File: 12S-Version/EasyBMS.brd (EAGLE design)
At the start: 49 x 100 mm, 146 parts, among them IC2 LTC6811IG-1#PBF, Q10 BSS84LT1G, Q11 BSS84LT1G, Q12 BSS84LT1G, Q13 BSS84LT1G, Q2 BSS84LT1G, Q3 BSS84LT1G, Q4 BSS84LT1G, Q5 BSS84LT1G, Q6 BSS84LT1G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

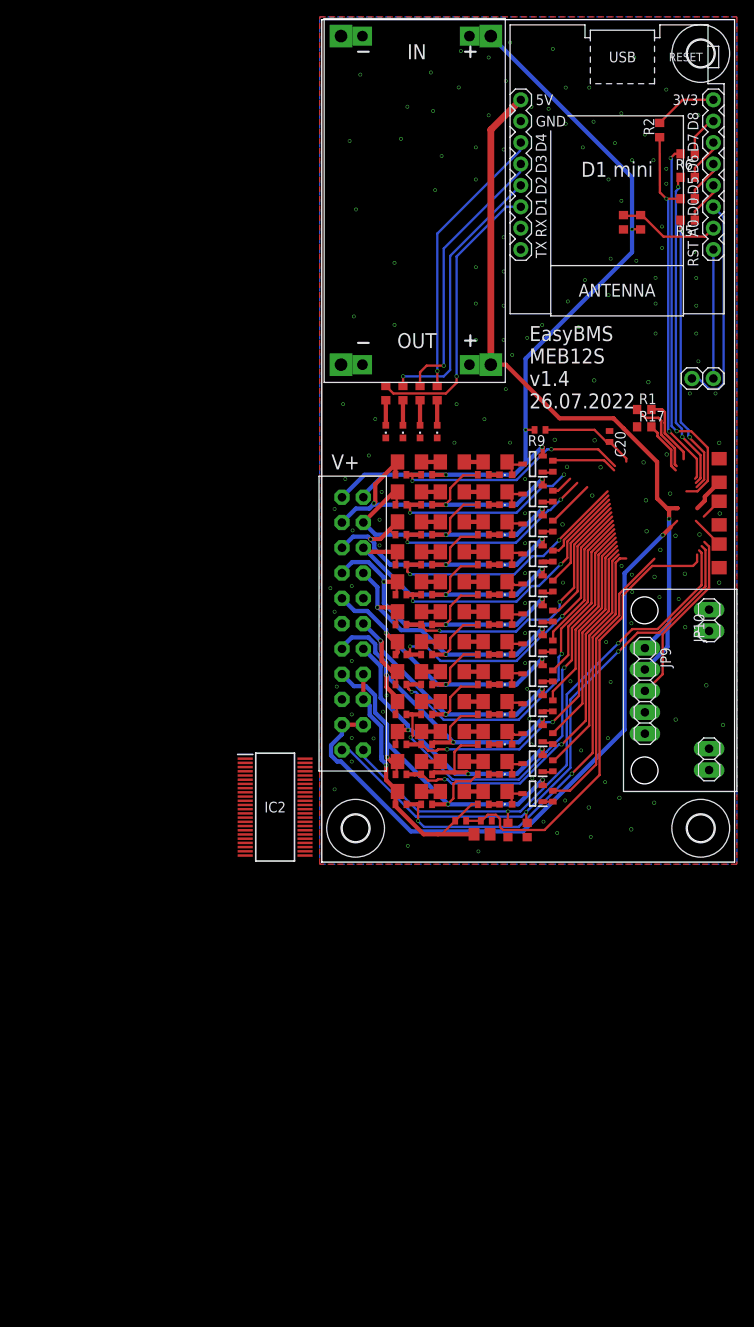
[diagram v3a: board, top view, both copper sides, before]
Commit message: add schematic for dc converter design
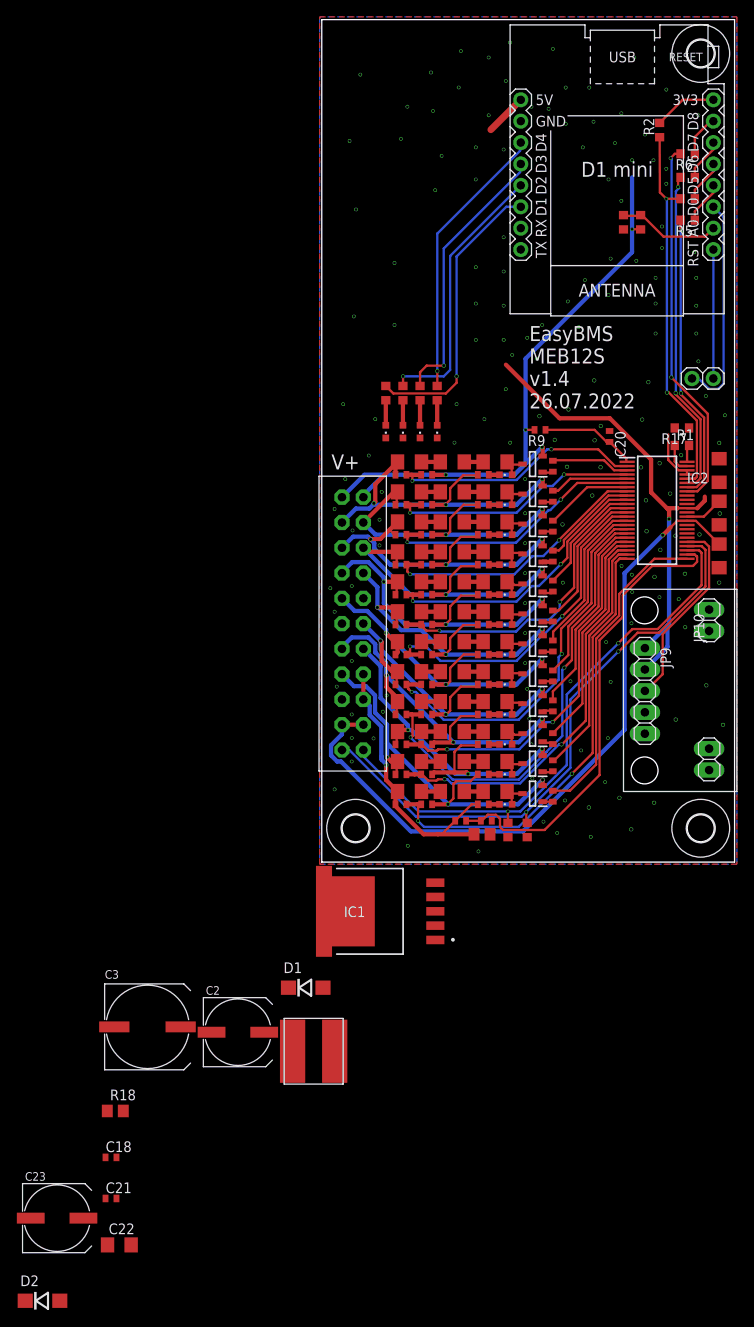
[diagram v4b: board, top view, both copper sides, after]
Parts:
- removed U$1: DC-DC-STEP-DOWN-LM2596HVS, diy-modules:DC-DC-STEP-DOWN-LM2596HVS
- added C18, C21: 100n, rcl:C0402
- added C2, C23: C249880, rcl:UD-8X10_NICHICON
- added C22: 1uF, rcl:C1206
- added C3: C249836, rcl:UD-10X10_NICHICON
- added D1, D2: C16015, diode:DO214BA
- added IC1: LM2596S-5.0_NOPB, SamacSys_Parts:KTT0005B
- added L1: C2929443, SamacSys_Parts:CY75-100UH
- added R18: C1017, rcl:R0805
- moved IC2 57.4 mm to (39.8, 41.8)
- moved R1 6.18 mm to (42.7, 49.5)
- moved R17 4.47 mm to (42.7, 51.5), turned to 180 degrees
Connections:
- new net +5V: C19.1, C22.1, C23.+, IC2.36, IC2.37, R18.2
- new net +5V/1: C2.+, C21.1, D2.A, IC1.4, L1.P$2, R18.1
- new net N$17: D1.C, IC1.2, L1.P$1
- new net N$25: D2.C, U$2.JP2.8
- net 5VDC: no longer C19.1, IC2.36, IC2.37, U$1.OUT+, U$2.JP2.8
- net C12+: now also C18.1, C3.+, IC1.1; no longer U$1.IN+
- net GND: now also C18.2, C2.-, C21.2, C22.2, C23.-, C3.-, D1.A, IC1.3, IC1.5, IC1.6; no longer U$1.IN-, U$1.OUT-
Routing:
- net 5VDC: track 94.3 -> 53.9 mm
- net C12+: track 97.7 -> 73.9 mm
- net C11: track 22.9 -> 30.4 mm
- net S11: track 2.64 -> 9.41 mm
- net IPB: track 8.25 -> 2.05 mm
- net IMB: track 9.56 -> 3.59 mm
- net C10: track 25.8 -> 31.7 mm
- net N$25: track 0.00 -> 5.03 mm
- net S10: track 5.72 -> 10.5 mm
- net S1: track 33.7 -> 37.6 mm
- net +5V: track 0.00 -> 2.97 mm
- net C9: track 30.6 -> 32.9 mm
- net S9: track 9.66 -> 11.9 mm
- net VREF2: track 81.6 -> 83.8 mm
- net C8: track 32.0 -> 34.1 mm
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
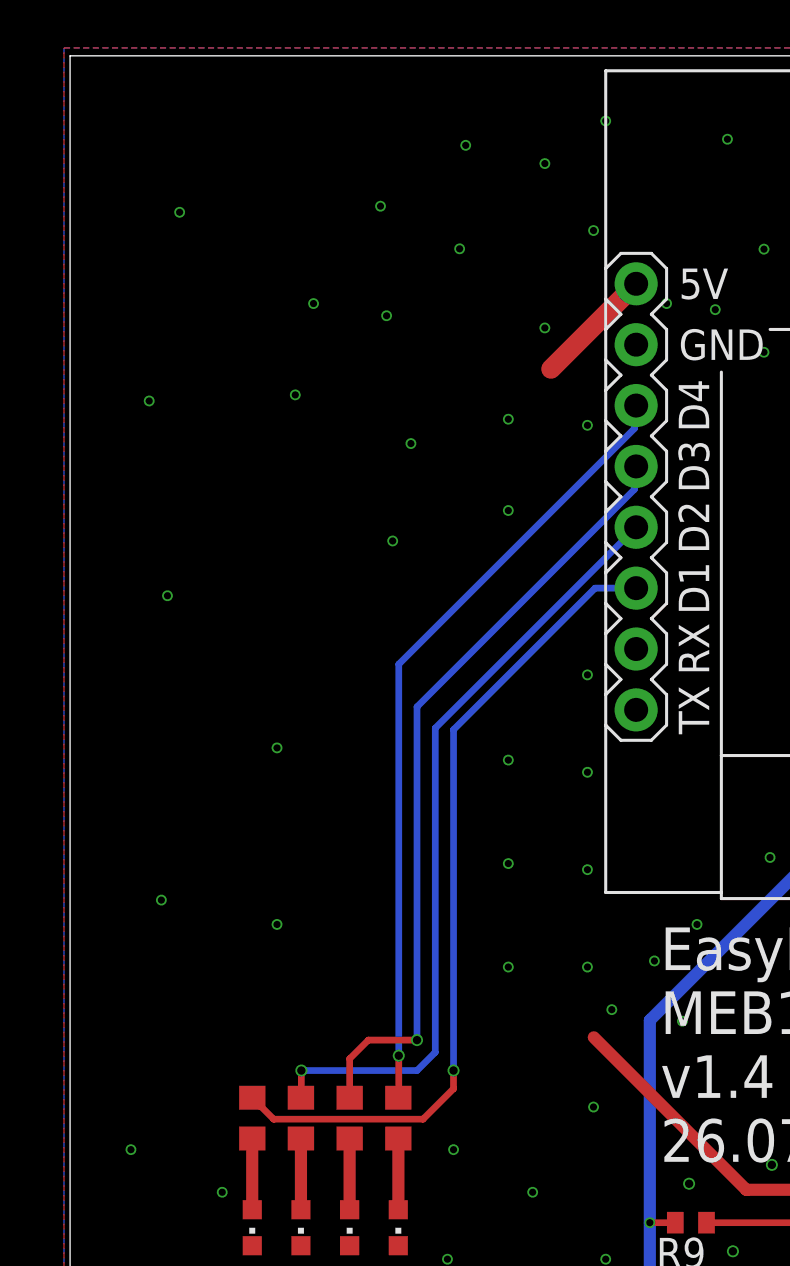
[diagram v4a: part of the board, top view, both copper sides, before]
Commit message: some traces removed
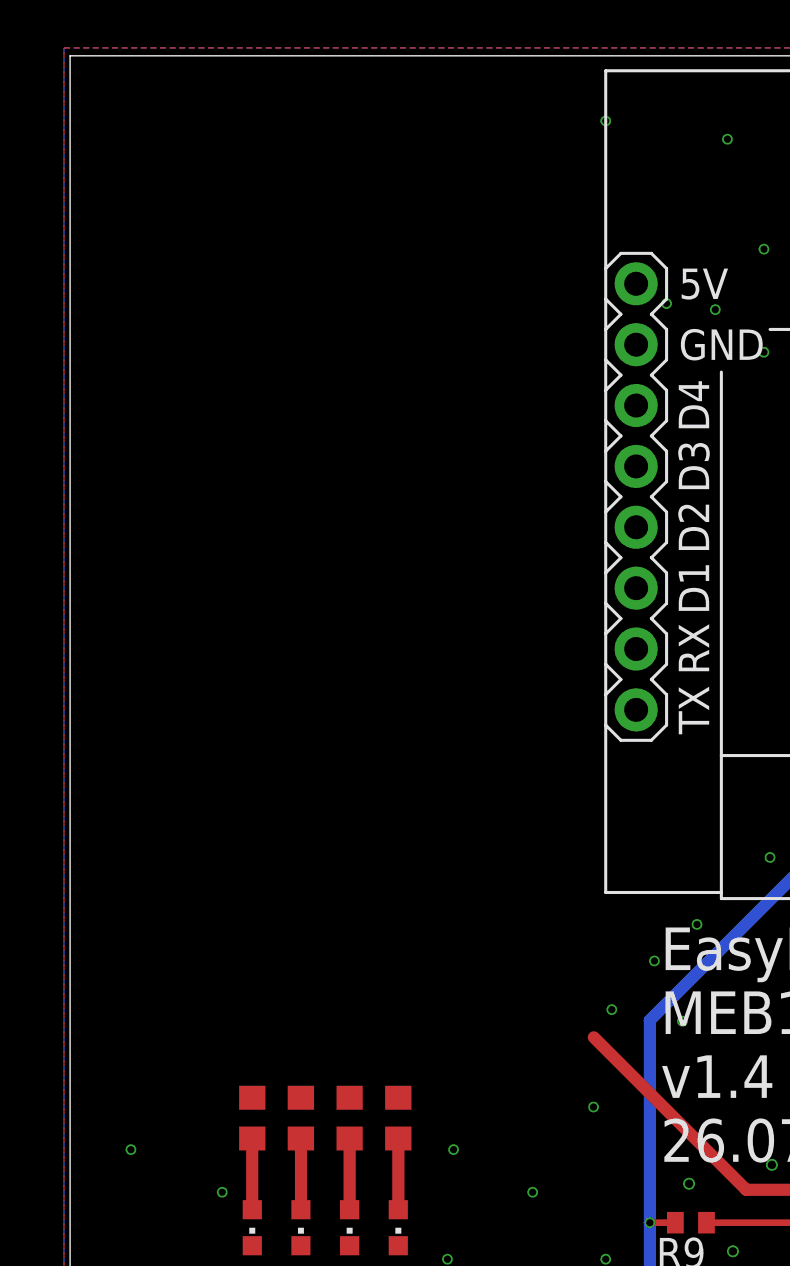
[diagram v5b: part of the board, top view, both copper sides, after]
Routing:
- net N$70: track 34.3 -> 0.00 mm, vias 1 -> 0
- net N$30: track 33.0 -> 0.00 mm, vias 1 -> 0
- net N$120: track 32.5 -> 0.00 mm, vias 1 -> 0
- net N$124: track 32.4 -> 0.00 mm, vias 1 -> 0
- net N$25: track 5.03 -> 0.00 mm
- net GND: vias 160 -> 133

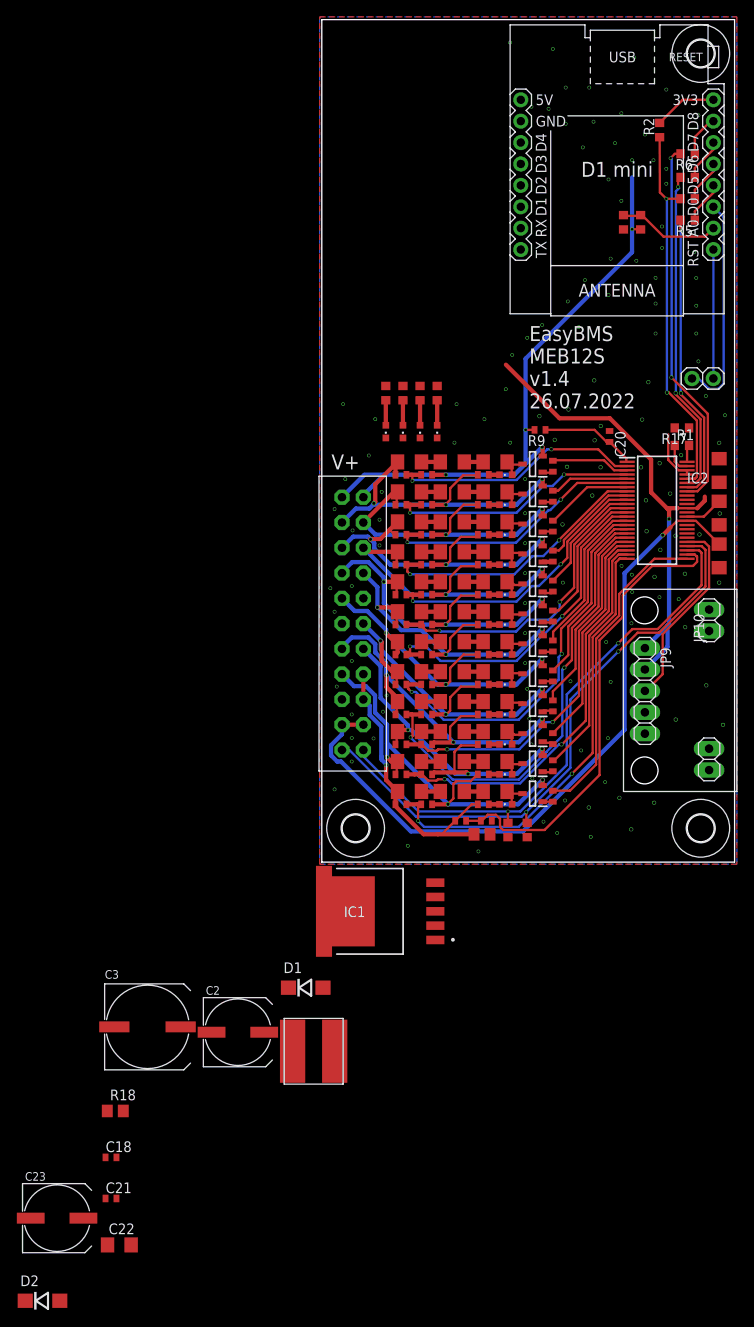
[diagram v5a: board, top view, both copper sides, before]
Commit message: new parts placed inside of the board for a first cost estimation on jlc
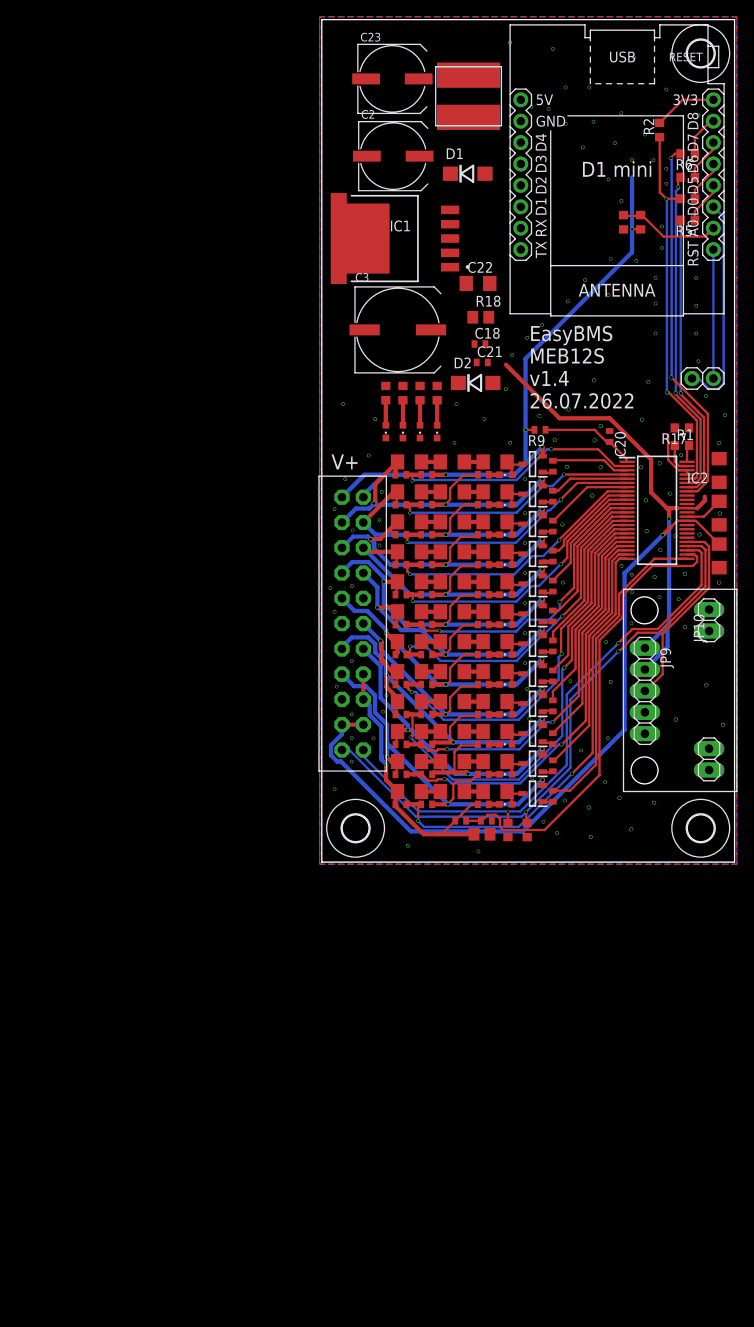
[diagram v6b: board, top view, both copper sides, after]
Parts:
- moved C23 141.0 mm to (8.38, 93.0)
- moved C22 121.8 mm to (18.5, 68.7)
- moved D2 120.5 mm to (18.3, 56.9)
- moved L1 114.8 mm to (17.4, 90.9), turned to 90 degrees
- moved C21 108.6 mm to (19.1, 59.3)
- moved C18 106.0 mm to (18.8, 61.5)
- moved C2 105.6 mm to (8.48, 83.8)
- moved R18 103.7 mm to (18.9, 64.7)
- moved D1 98.5 mm to (17.3, 81.7)
- moved C3 87.9 mm to (9.04, 63.2)
- moved IC1 79.9 mm to (2.77, 74.0)

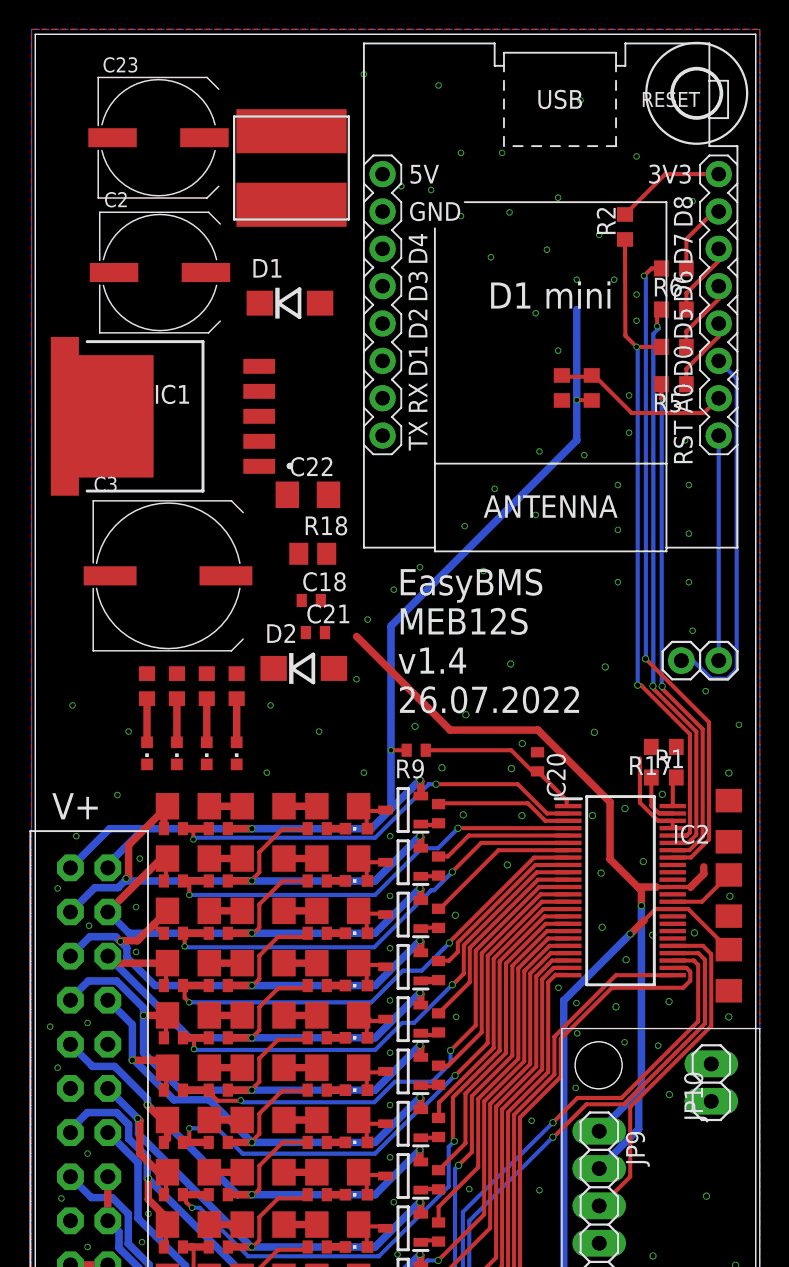
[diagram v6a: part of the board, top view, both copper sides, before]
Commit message: layout with integrated dc/dc is ready, changed input capacitor to a larger one
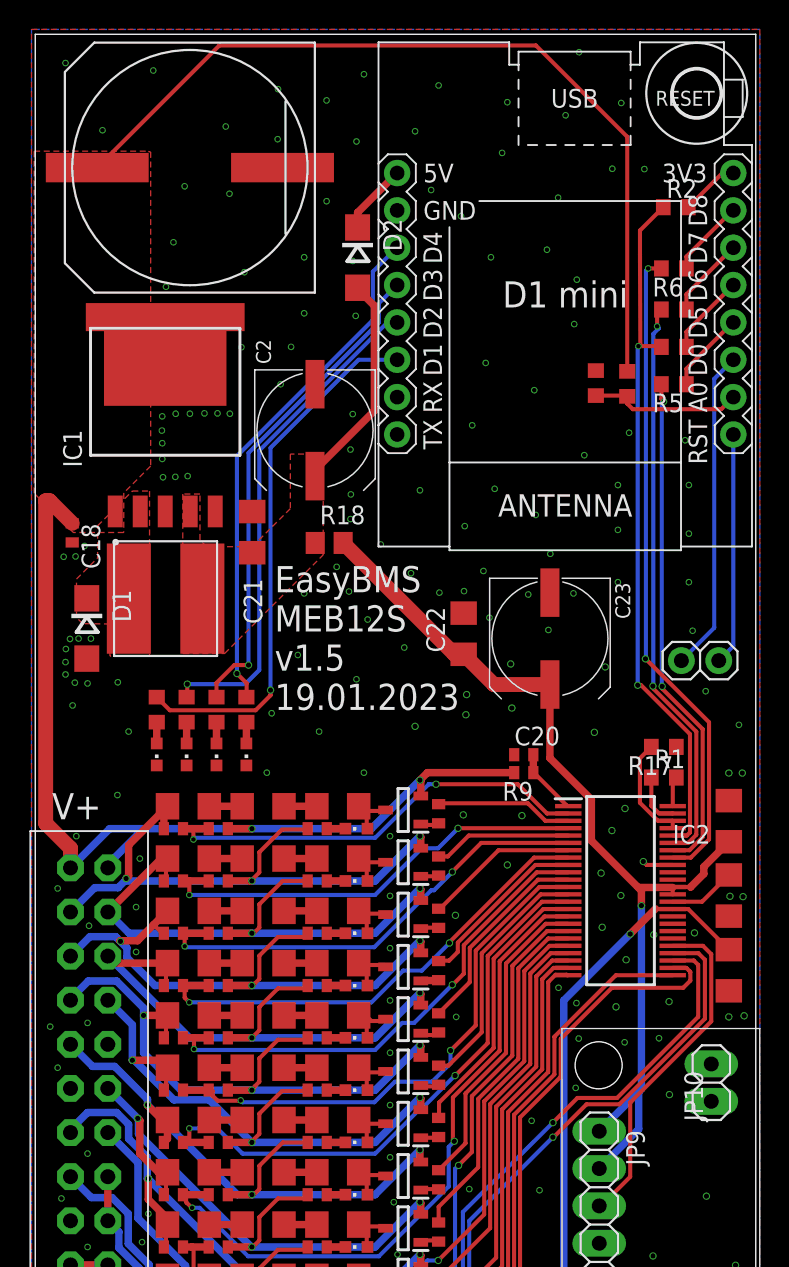
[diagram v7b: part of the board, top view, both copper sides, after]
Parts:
- removed C3: C249836, rcl:UD-10X10_NICHICON
- added C24: C249935, SamacSys_Parts:VZH471M1JTR-1616
- C21: value 100n -> 1uF; device rcl:C0402 -> rcl:C1206
- D1, D2: device diode:DO214BA -> diode:DO214AC
- moved C23 43.2 mm to (35.0, 58.9), turned to 270 degrees
- moved L1 30.5 mm to (8.86, 61.6), turned to 0 degrees
- moved D2 28.2 mm to (21.9, 84.8), turned to 270 degrees
- moved D1 26.1 mm to (3.51, 59.6), turned to 270 degrees
- moved C18 16.9 mm to (2.51, 66.1), turned to 270 degrees
- moved C2 15.0 mm to (19.0, 73.1), turned to 270 degrees
- moved C22 14.2 mm to (29.1, 59.2), turned to 90 degrees
- moved C21 8.07 mm to (14.8, 66.1), turned to 90 degrees
- moved R9 7.47 mm to (33.2, 49.8)
- moved IC1 6.08 mm to (8.84, 73.7), turned to 270 degrees
- moved R2 3.71 mm to (43.6, 88.2), turned to 0 degrees
- moved R15 2.43 mm to (40.3, 76.2), turned to 90 degrees
- moved R16 2.33 mm to (38.1, 76.3), turned to 270 degrees
- moved R53 1.73 mm to (8.26, 54.1)
- moved R54 1.73 mm to (10.3, 54.1)
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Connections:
- removed net 5VDC: JP9.1, JP9.2
- net +5V: now also JP9.1, JP9.2
- net C12+: now also C24.+; no longer C3.+
- net GND: now also C24.-, IC1.7, IC1.8; no longer C3.-
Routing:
- net +5V: track 2.97 -> 66.8 mm, vias 0 -> 1
- net 5VDC: track 53.9 -> 0.00 mm, vias 1 -> 0
- net C12+: track 73.9 -> 125.4 mm, vias 4 -> 2
- net N$70: track 0.00 -> 36.5 mm, vias 0 -> 1
- net N$30: track 0.00 -> 35.4 mm, vias 0 -> 1
- net N$124: track 0.00 -> 34.1 mm, vias 0 -> 1
- net N$120: track 0.00 -> 33.7 mm, vias 0 -> 1
- net +5V/1: track 0.00 -> 15.0 mm
- net V+: track 11.4 -> 4.48 mm
- net N$25: track 0.00 -> 4.82 mm
- net N$6: track 26.0 -> 21.9 mm
- net +3V3: track 7.51 -> 4.02 mm
- net MISO: track 45.2 -> 47.7 mm
- net GND: track 0.75 -> 2.85 mm, vias 133 -> 193
- net A0IN: track 11.9 -> 10.4 mm
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- added copper zone on layer 1, net +5V/1
- added copper zone on layer 1, net C12+
- added copper zone on layer 1, net N$17
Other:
- board text added: "EasyBMS MEB12S v1.5 19.01.2023"
- board text removed: "EasyBMS MEB12S v1.4 26.07.2022"
